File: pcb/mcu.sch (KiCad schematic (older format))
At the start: 33 parts, among them J4 SWD Programming Header, J5 Conn_01x16_Male, J6 Conn_01x16_Male, Q1 2N7002, Q2 2N7002, Q3 2N7002, Q4 2N7002, SW1 Rotary_Encoder_Switch, U2 LM1117-3.3, U3 ﻿STM32L010C6

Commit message: PCB updates
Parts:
- added R7, R9: 10k, Resistor_SMD:R_0603_1608Metric, symbol Device:R
- added TP1: TestPoint, TestPoint:TestPoint_Pad_2.0x2.0mm, symbol Connector:TestPoint
- C18, C20, C21: value C -> 10n
- J5, J6: footprint Connector_PinHeader_2.54mm:PinHeader_1x16_P2.54mm_Vertical -> Connector_PinHeader_2.54mm:PinHeader_2x08_P2.54mm_Vertical
- R2, R3, R4: value R -> 10k; footprint (none) -> Resistor_SMD:R_0603_1608Metric
- SW1: footprint (none) -> Rotary_Encoder:RotaryEncoder_Alps_EC11E-Switch_Vertical_H20mm_CircularMountingHoles
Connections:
- net +3V3: now also R7.2, R9.2; no longer C18.1
- net GND: now also C18.2
- net SW: now also C18.1; no longer C18.2
- net ~RST: now also TP1.1
- net at R4.2, SW1.A: now also R9.1
- net at R3.2, SW1.B: now also R7.1
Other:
- moved on the sheet: C18
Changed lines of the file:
@@
 $Descr A4 11693 8268
 encoding utf-8
-Sheet 3 3
+Sheet 3 4
 Title ""
 Date ""
@@
 F 0 "SW1" H 2250 5083 50  0000 C CNN
 F 1 "Rotary_Encoder_Switch" H 2250 5174 50  0000 C CNN
-F 2 "" H 2100 5610 50  0001 C CNN
+F 2 "Rotary_Encoder:RotaryEncoder_Alps_EC11E-Switch_Vertical_H20mm_CircularMountingHoles" H 2100 5610 50  0001 C CNN
 F 3 "~" H 2250 5710 50  0001 C CNN
 	1    2250 5450
@@
 P 2950 5350
 F 0 "R3" V 2743 5350 50  0000 C CNN
-F 1 "R" V 2834 5350 50  0000 C CNN
-F 2 "" V 2880 5350 50  0001 C CNN
+F 1 "10k" V 2834 5350 50  0000 C CNN
+F 2 "Resistor_SMD:R_0603_1608Metric" V 2880 5350 50  0001 C CNN
 F 3 "~" H 2950 5350 50  0001 C CNN
 	1    2950 5350
@@
 P 2950 5550
 F 0 "R4" V 2743 5550 50  0000 C CNN
-F 1 "R" V 2834 5550 50  0000 C CNN
-F 2 "" V 2880 5550 50  0001 C CNN
+F 1 "10k" V 2834 5550 50  0000 C CNN
+F 2 "Resistor_SMD:R_0603_1608Metric" V 2880 5550 50  0001 C CNN
 F 3 "~" H 2950 5550 50  0001 C CNN
 	1    2950 5550
@@
 $EndComp
 Wire Wire Line
-	2550 5350 2800 5350
-Wire Wire Line
-	2550 5550 2800 5550
+	2550 5350 2600 5350
+Wire Wire Line
+	2550 5550 2700 5550
 $Comp
 L Device:C C20
@@
 P 3200 5700
 F 0 "C20" H 3315 5746 50  0000 L CNN
-F 1 "C" H 3315 5655 50  0000 L CNN
+F 1 "10n" H 3315 5655 50  0000 L CNN
 F 2 "Capacitor_SMD:C_0603_1608Metric" H 3238 5550 50  0001 C CNN
 F 3 "~" H 3200 5700 50  0001 C CNN
@@
 P 3600 5700
 F 0 "C21" H 3715 5746 50  0000 L CNN
-F 1 "C" H 3715 5655 50  0000 L CNN
+F 1 "10n" H 3715 5655 50  0000 L CNN
 F 2 "Capacitor_SMD:C_0603_1608Metric" H 3638 5550 50  0001 C CNN
 F 3 "~" H 3600 5700 50  0001 C CNN
@@
 P 1800 5000
 F 0 "R2" H 1730 4954 50  0000 R CNN
-F 1 "R" H 1730 5045 50  0000 R CNN
-F 2 "" V 1730 5000 50  0001 C CNN
+F 1 "10k" H 1730 5045 50  0000 R CNN
+F 2 "Resistor_SMD:R_0603_1608Metric" V 1730 5000 50  0001 C CNN
 F 3 "~" H 1800 5000 50  0001 C CNN
 	1    1800 5000
@@
 L Device:C C18
 U 1 1 61337D20
-P 1500 5000
-F 0 "C18" H 1615 5046 50  0000 L CNN
-F 1 "C" H 1615 4955 50  0000 L CNN
-F 2 "Capacitor_SMD:C_0603_1608Metric" H 1538 4850 50  0001 C CNN
-F 3 "~" H 1500 5000 50  0001 C CNN
-	1    1500 5000
+P 1650 5500
+F 0 "C18" H 1765 5546 50  0000 L CNN
+F 1 "10n" H 1765 5455 50  0000 L CNN
+F 2 "Capacitor_SMD:C_0603_1608Metric" H 1688 5350 50  0001 C CNN
+F 3 "~" H 1650 5500 50  0001 C CNN
+	1    1650 5500
 	1    0    0    -1
 $EndComp
@@
 Wire Wire Line
 	1800 5350 1800 5150
-Wire Wire Line
-	1500 5150 1800 5150
-Wire Wire Line
-	1500 4850 1800 4850
 $Comp
 L power:+3.3V #PWR023
@@
 	1    0    0    -1
 $EndComp
-Connection ~ 1800 4850
 Text Label 1500 5350 0    50   ~ 0
 SW
 Wire Wire Line
-	1500 5350 1800 5350
+	1500 5350 1650 5350
 Connection ~ 1800 5350
 Text Label 3150 5550 0    50   ~ 0
@@
 F 0 "J6" H 7422 3724 50  0000 R CNN
 F 1 "Conn_01x16_Male" H 7422 3633 50  0000 R CNN
-F 2 "Connector_PinHeader_2.54mm:PinHeader_1x16_P2.54mm_Vertical" H 7450 3750 50  0001 C CNN
+F 2 "Connector_PinHeader_2.54mm:PinHeader_2x08_P2.54mm_Vertical" H 7450 3750 50  0001 C CNN
 F 3 "~" H 7450 3750 50  0001 C CNN
 	1    7450 3750
@@
 Wire Wire Line
 	7250 4550 6700 4550
-Connection ~ 1800 5150
 $Comp
 L Connector:Conn_01x16_Male J5
@@
 F 0 "J5" H 3608 4631 50  0000 C CNN
 F 1 "Conn_01x16_Male" H 3608 4540 50  0000 C CNN
-F 2 "Connector_PinHeader_2.54mm:PinHeader_1x16_P2.54mm_Vertical" H 3500 3750 50  0001 C CNN
+F 2 "Connector_PinHeader_2.54mm:PinHeader_2x08_P2.54mm_Vertical" H 3500 3750 50  0001 C CNN
 F 3 "~" H 3500 3750 50  0001 C CNN
 	1    3500 3750
@@
 Wire Wire Line
 	4200 1650 4450 1650
+$Comp
+L Connector:TestPoint TP1
+U 1 1 613DAC52
+P 5800 1350
+F 0 "TP1" H 5858 1468 50  0000 L CNN
+F 1 "TestPoint" H 5858 1377 50  0000 L CNN
+F 2 "TestPoint:TestPoint_Pad_2.0x2.0mm" H 6000 1350 50  0001 C CNN
+F 3 "~" H 6000 1350 50  0001 C CNN
+	1    5800 1350
+	1    0    0    -1
+$EndComp
+$Comp
+L Device:R R7
+U 1 1 613E9042
+P 2600 5200
+F 0 "R7" V 2393 5200 50  0000 C CNN
+F 1 "10k" V 2484 5200 50  0000 C CNN
+F 2 "Resistor_SMD:R_0603_1608Metric" V 2530 5200 50  0001 C CNN
+F 3 "~" H 2600 5200 50  0001 C CNN
+	1    2600 5200
+	-1   0    0    1
+$EndComp
+Connection ~ 2600 5350
+Wire Wire Line
+	2600 5350 2800 5350
+$Comp
+L Device:R R9
+U 1 1 613E96FC
+P 2700 5400
+F 0 "R9" V 2493 5400 50  0000 C CNN
+F 1 "10k" V 2584 5400 50  0000 C CNN
+F 2 "Resistor_SMD:R_0603_1608Metric" V 2630 5400 50  0001 C CNN
+F 3 "~" H 2700 5400 50  0001 C CNN
+	1    2700 5400
+	-1   0    0    1
+$EndComp
+Connection ~ 2700 5550
+Wire Wire Line
+	2700 5550 2800 5550
+$Comp
+L power:+3.3V #PWR0103
+U 1 1 613EA3BC
+P 2600 4900
+F 0 "#PWR0103" H 2600 4750 50  0001 C CNN
+F 1 "+3.3V" H 2615 5073 50  0000 C CNN
+F 2 "" H 2600 4900 50  0001 C CNN
+F 3 "" H 2600 4900 50  0001 C CNN
+	1    2600 4900
+	1    0    0    -1
+$EndComp
+Wire Wire Line
+	2600 5050 2600 4900
+Wire Wire Line
+	2700 5250 2700 4900
+Wire Wire Line
+	2700 4900 2600 4900
+Connection ~ 2600 4900
+Connection ~ 1650 5350
+Wire Wire Line
+	1650 5350 1800 5350
+Wire Wire Line
+	1650 5650 1750 5650
+Wire Wire Line
+	1750 5650 1750 5600
+Wire Wire Line
+	1750 5600 1800 5600
+Connection ~ 1800 5600
 $EndSCHEMATC

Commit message: layout check in
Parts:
- removed J5, J6: Conn_01x16_Male, Connector_PinHeader_2.54mm:PinHeader_2x08_P2.54mm_Vertical, symbol Connector:Conn_01x16_Male
- added J5: Conn_02x04_Odd_Even, Connector_PinHeader_2.54mm:PinHeader_2x04_P2.54mm_Vertical, symbol Connector_Generic:Conn_02x04_Odd_Even
- C17, C18, C19, C20, C21, C22, C23, C24, C25: footprint Capacitor_SMD:C_0603_1608Metric -> Capacitor_SMD:C_0402_1005Metric
- R10, R12, R14, R15, R16, R17, R18, R2, R3, R4, R5, R6, R7, R8, R9: footprint Resistor_SMD:R_0603_1608Metric -> Resistor_SMD:R_0402_1005Metric
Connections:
- wire segments 81 -> 103
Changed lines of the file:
@@
 F 0 "C19" H 2365 1246 50  0000 L CNN
 F 1 "1u" H 2365 1155 50  0000 L CNN
-F 2 "Capacitor_SMD:C_0603_1608Metric" H 2288 1050 50  0001 C CNN
+F 2 "Capacitor_SMD:C_0402_1005Metric" H 2288 1050 50  0001 C CNN
 F 3 "~" H 2250 1200 50  0001 C CNN
 	1    2250 1200
@@
 F 0 "C17" H 1365 1246 50  0000 L CNN
 F 1 "1u" H 1365 1155 50  0000 L CNN
-F 2 "Capacitor_SMD:C_0603_1608Metric" H 1288 1050 50  0001 C CNN
+F 2 "Capacitor_SMD:C_0402_1005Metric" H 1288 1050 50  0001 C CNN
 F 3 "~" H 1250 1200 50  0001 C CNN
 	1    1250 1200
@@
 F 0 "C23" H 4815 1546 50  0000 L CNN
 F 1 "100n" H 4815 1455 50  0000 L CNN
-F 2 "Capacitor_SMD:C_0603_1608Metric" H 4738 1350 50  0001 C CNN
+F 2 "Capacitor_SMD:C_0402_1005Metric" H 4738 1350 50  0001 C CNN
 F 3 "~" H 4700 1500 50  0001 C CNN
 	1    4700 1500
@@
 F 0 "C22" H 4565 1546 50  0000 L CNN
 F 1 "100n" H 4565 1455 50  0000 L CNN
-F 2 "Capacitor_SMD:C_0603_1608Metric" H 4488 1350 50  0001 C CNN
+F 2 "Capacitor_SMD:C_0402_1005Metric" H 4488 1350 50  0001 C CNN
 F 3 "~" H 4450 1500 50  0001 C CNN
 	1    4450 1500
@@
 F 0 "R3" V 2743 5350 50  0000 C CNN
 F 1 "10k" V 2834 5350 50  0000 C CNN
-F 2 "Resistor_SMD:R_0603_1608Metric" V 2880 5350 50  0001 C CNN
+F 2 "Resistor_SMD:R_0402_1005Metric" V 2880 5350 50  0001 C CNN
 F 3 "~" H 2950 5350 50  0001 C CNN
 	1    2950 5350
@@
 F 0 "R4" V 2743 5550 50  0000 C CNN
 F 1 "10k" V 2834 5550 50  0000 C CNN
-F 2 "Resistor_SMD:R_0603_1608Metric" V 2880 5550 50  0001 C CNN
+F 2 "Resistor_SMD:R_0402_1005Metric" V 2880 5550 50  0001 C CNN
 F 3 "~" H 2950 5550 50  0001 C CNN
 	1    2950 5550
@@
 F 0 "C20" H 3315 5746 50  0000 L CNN
 F 1 "10n" H 3315 5655 50  0000 L CNN
-F 2 "Capacitor_SMD:C_0603_1608Metric" H 3238 5550 50  0001 C CNN
+F 2 "Capacitor_SMD:C_0402_1005Metric" H 3238 5550 50  0001 C CNN
 F 3 "~" H 3200 5700 50  0001 C CNN
 	1    3200 5700
@@
 F 0 "C21" H 3715 5746 50  0000 L CNN
 F 1 "10n" H 3715 5655 50  0000 L CNN
-F 2 "Capacitor_SMD:C_0603_1608Metric" H 3638 5550 50  0001 C CNN
+F 2 "Capacitor_SMD:C_0402_1005Metric" H 3638 5550 50  0001 C CNN
 F 3 "~" H 3600 5700 50  0001 C CNN
 	1    3600 5700
@@
 F 0 "R2" H 1730 4954 50  0000 R CNN
 F 1 "10k" H 1730 5045 50  0000 R CNN
-F 2 "Resistor_SMD:R_0603_1608Metric" V 1730 5000 50  0001 C CNN
+F 2 "Resistor_SMD:R_0402_1005Metric" V 1730 5000 50  0001 C CNN
 F 3 "~" H 1800 5000 50  0001 C CNN
 	1    1800 5000
@@
 F 0 "C18" H 1765 5546 50  0000 L CNN
 F 1 "10n" H 1765 5455 50  0000 L CNN
-F 2 "Capacitor_SMD:C_0603_1608Metric" H 1688 5350 50  0001 C CNN
+F 2 "Capacitor_SMD:C_0402_1005Metric" H 1688 5350 50  0001 C CNN
 F 3 "~" H 1650 5500 50  0001 C CNN
 	1    1650 5500
@@
 F 0 "C24" H 5765 1546 50  0000 L CNN
 F 1 "0.1u" H 5765 1455 50  0000 L CNN
-F 2 "Capacitor_SMD:C_0603_1608Metric" H 5688 1350 50  0001 C CNN
+F 2 "Capacitor_SMD:C_0402_1005Metric" H 5688 1350 50  0001 C CNN
 F 3 "~" H 5650 1500 50  0001 C CNN
 	1    5650 1500
@@
 F 0 "R5" H 9320 1246 50  0000 L CNN
 F 1 "82" H 9320 1155 50  0000 L CNN
-F 2 "Resistor_SMD:R_0603_1608Metric" V 9180 1200 50  0001 C CNN
+F 2 "Resistor_SMD:R_0402_1005Metric" V 9180 1200 50  0001 C CNN
 F 3 "~" H 9250 1200 50  0001 C CNN
 	1    9250 1200
@@
 F 0 "R6" H 9420 1246 50  0000 L CNN
 F 1 "82" H 9420 1155 50  0000 L CNN
-F 2 "Resistor_SMD:R_0603_1608Metric" V 9280 1200 50  0001 C CNN
+F 2 "Resistor_SMD:R_0402_1005Metric" V 9280 1200 50  0001 C CNN
 F 3 "~" H 9350 1200 50  0001 C CNN
 	1    9350 1200
@@
 F 0 "R8" H 9520 1246 50  0000 L CNN
 F 1 "82" H 9520 1155 50  0000 L CNN
-F 2 "Resistor_SMD:R_0603_1608Metric" V 9380 1200 50  0001 C CNN
+F 2 "Resistor_SMD:R_0402_1005Metric" V 9380 1200 50  0001 C CNN
 F 3 "~" H 9450 1200 50  0001 C CNN
 	1    9450 1200
@@
 F 0 "R10" H 9620 1246 50  0000 L CNN
 F 1 "82" H 9620 1155 50  0000 L CNN
-F 2 "Resistor_SMD:R_0603_1608Metric" V 9480 1200 50  0001 C CNN
+F 2 "Resistor_SMD:R_0402_1005Metric" V 9480 1200 50  0001 C CNN
 F 3 "~" H 9550 1200 50  0001 C CNN
 	1    9550 1200
@@
 F 0 "R12" H 9720 1246 50  0000 L CNN
 F 1 "82" H 9720 1155 50  0000 L CNN
-F 2 "Resistor_SMD:R_0603_1608Metric" V 9580 1200 50  0001 C CNN
+F 2 "Resistor_SMD:R_0402_1005Metric" V 9580 1200 50  0001 C CNN
 F 3 "~" H 9650 1200 50  0001 C CNN
 	1    9650 1200
@@
 F 0 "R14" H 9820 1246 50  0000 L CNN
 F 1 "82" H 9820 1155 50  0000 L CNN
-F 2 "Resistor_SMD:R_0603_1608Metric" V 9680 1200 50  0001 C CNN
+F 2 "Resistor_SMD:R_0402_1005Metric" V 9680 1200 50  0001 C CNN
 F 3 "~" H 9750 1200 50  0001 C CNN
 	1    9750 1200
@@
 F 0 "R15" H 9920 1246 50  0000 L CNN
 F 1 "82" H 9920 1155 50  0000 L CNN
-F 2 "Resistor_SMD:R_0603_1608Metric" V 9780 1200 50  0001 C CNN
+F 2 "Resistor_SMD:R_0402_1005Metric" V 9780 1200 50  0001 C CNN
 F 3 "~" H 9850 1200 50  0001 C CNN
 	1    9850 1200
@@
 F 0 "R16" H 10020 1246 50  0000 L CNN
 F 1 "82" H 10020 1155 50  0000 L CNN
-F 2 "Resistor_SMD:R_0603_1608Metric" V 9880 1200 50  0001 C CNN
+F 2 "Resistor_SMD:R_0402_1005Metric" V 9880 1200 50  0001 C CNN
 F 3 "~" H 9950 1200 50  0001 C CNN
 	1    9950 1200
@@
 F 0 "R17" H 10120 1246 50  0000 L CNN
 F 1 "82" H 10120 1155 50  0000 L CNN
-F 2 "Resistor_SMD:R_0603_1608Metric" V 9980 1200 50  0001 C CNN
+F 2 "Resistor_SMD:R_0402_1005Metric" V 9980 1200 50  0001 C CNN
 F 3 "~" H 10050 1200 50  0001 C CNN
 	1    10050 1200
@@
 F 0 "R18" H 10220 1246 50  0000 L CNN
 F 1 "82" H 10220 1155 50  0000 L CNN
-F 2 "Resistor_SMD:R_0603_1608Metric" V 10080 1200 50  0001 C CNN
+F 2 "Resistor_SMD:R_0402_1005Metric" V 10080 1200 50  0001 C CNN
 F 3 "~" H 10150 1200 50  0001 C CNN
 	1    10150 1200
@@
 Text Label 6700 4350 0    50   ~ 0
 DIG4
-$Comp
-L Connector:Conn_01x16_Male J6
-U 1 1 613A74A3
-P 7450 3750
-F 0 "J6" H 7422 3724 50  0000 R CNN
-F 1 "Conn_01x16_Male" H 7422 3633 50  0000 R CNN
-F 2 "Connector_PinHeader_2.54mm:PinHeader_2x08_P2.54mm_Vertical" H 7450 3750 50  0001 C CNN
-F 3 "~" H 7450 3750 50  0001 C CNN
-	1    7450 3750
-	-1   0    0    -1
-$EndComp
 Wire Wire Line
 	7250 3050 6700 3050
@@
 Wire Wire Line
 	7250 4550 6700 4550
-$Comp
-L Connector:Conn_01x16_Male J5
-U 1 1 613C1375
-P 3500 3750
-F 0 "J5" H 3608 4631 50  0000 C CNN
-F 1 "Conn_01x16_Male" H 3608 4540 50  0000 C CNN
-F 2 "Connector_PinHeader_2.54mm:PinHeader_2x08_P2.54mm_Vertical" H 3500 3750 50  0001 C CNN
-F 3 "~" H 3500 3750 50  0001 C CNN
-	1    3500 3750
-	1    0    0    -1
-$EndComp
-Wire Wire Line
-	3700 3050 4600 3050
-Wire Wire Line
-	3700 3150 4600 3150
-Wire Wire Line
-	4600 3250 3700 3250
-Wire Wire Line
-	3700 3350 4600 3350
-Wire Wire Line
-	4600 3450 3700 3450
-Wire Wire Line
-	3700 3550 4600 3550
-Wire Wire Line
-	3700 3650 4600 3650
-Wire Wire Line
-	4600 3750 3700 3750
 Wire Wire Line
 	3700 3850 4600 3850
 Wire Wire Line
 	4600 3950 3700 3950
-Wire Wire Line
-	3700 4050 4600 4050
-Wire Wire Line
-	4600 4150 3700 4150
-Wire Wire Line
-	3700 4250 4600 4250
-Wire Wire Line
-	3700 4350 4600 4350
-Wire Wire Line
-	3700 4450 4600 4450
-Wire Wire Line
-	3750 4550 4600 4550
 $Comp
 L Device:C C25
@@
 F 0 "C25" H 4315 1546 50  0000 L CNN
 F 1 "100n" H 4315 1455 50  0000 L CNN
-F 2 "Capacitor_SMD:C_0603_1608Metric" H 4238 1350 50  0001 C CNN
+F 2 "Capacitor_SMD:C_0402_1005Metric" H 4238 1350 50  0001 C CNN
 F 3 "~" H 4200 1500 50  0001 C CNN
 	1    4200 1500
@@
 F 0 "R7" V 2393 5200 50  0000 C CNN
 F 1 "10k" V 2484 5200 50  0000 C CNN
-F 2 "Resistor_SMD:R_0603_1608Metric" V 2530 5200 50  0001 C CNN
+F 2 "Resistor_SMD:R_0402_1005Metric" V 2530 5200 50  0001 C CNN
 F 3 "~" H 2600 5200 50  0001 C CNN
 	1    2600 5200
@@
 F 0 "R9" V 2493 5400 50  0000 C CNN
 F 1 "10k" V 2584 5400 50  0000 C CNN
-F 2 "Resistor_SMD:R_0603_1608Metric" V 2630 5400 50  0001 C CNN
+F 2 "Resistor_SMD:R_0402_1005Metric" V 2630 5400 50  0001 C CNN
 F 3 "~" H 2700 5400 50  0001 C CNN
 	1    2700 5400
@@
 	1750 5600 1800 5600
 Connection ~ 1800 5600
+Wire Wire Line
+	2600 3550 4600 3550
+Wire Wire Line
+	2700 3650 4600 3650
+Wire Wire Line
+	2800 3750 2800 3850
+Wire Wire Line
+	2800 3750 4600 3750
+Wire Wire Line
+	2700 3650 2700 3850
+Wire Wire Line
+	2600 3550 2600 3850
+Wire Wire Line
+	2600 4350 2600 4600
+Wire Wire Line
+	2600 4600 3700 4600
+Wire Wire Line
+	3700 4600 3700 4550
+Wire Wire Line
+	2700 4550 2700 4350
+Wire Wire Line
+	2800 4350 2800 4500
+Wire Wire Line
+	3700 3850 3700 3800
+Wire Wire Line
+	3700 3800 2900 3800
+Wire Wire Line
+	2900 3800 2900 3850
+Wire Wire Line
+	4300 4350 4600 4350
+Wire Wire Line
+	4600 4450 4300 4450
+Wire Wire Line
+	4600 3050 4350 3050
+Wire Wire Line
+	4600 3150 4350 3150
+Wire Wire Line
+	3650 4250 3650 4550
+Wire Wire Line
+	3650 4550 2700 4550
+Wire Wire Line
+	3650 4250 3800 4250
+Wire Wire Line
+	2800 4500 3600 4500
+Wire Wire Line
+	3600 4500 3600 4150
+Wire Wire Line
+	3400 4050 3400 4450
+Wire Wire Line
+	3400 4450 2900 4450
+Wire Wire Line
+	2900 4450 2900 4350
+$Comp
+L Connector_Generic:Conn_02x04_Odd_Even J5
+U 1 1 6155CAFE
+P 2700 4150
+F 0 "J5" V 2796 3862 50  0000 R CNN
+F 1 "Conn_02x04_Odd_Even" V 2705 3862 50  0000 R CNN
+F 2 "Connector_PinHeader_2.54mm:PinHeader_2x04_P2.54mm_Vertical" H 2700 4150 50  0001 C CNN
+F 3 "~" H 2700 4150 50  0001 C CNN
+	1    2700 4150
+	0    -1   -1   0
+$EndComp
+Wire Wire Line
+	3700 4050 3700 3950
+Wire Wire Line
+	3400 4050 3700 4050
+Wire Wire Line
+	4600 4050 3750 4050
+Wire Wire Line
+	3750 4050 3750 4150
+Wire Wire Line
+	3750 4150 3600 4150
+Wire Wire Line
+	4600 4150 3800 4150
+Wire Wire Line
+	3800 4150 3800 4250
+Wire Wire Line
+	3700 4550 3850 4550
+Wire Wire Line
+	4600 4250 3850 4250
+Wire Wire Line
+	3850 4250 3850 4550
 $EndSCHEMATC

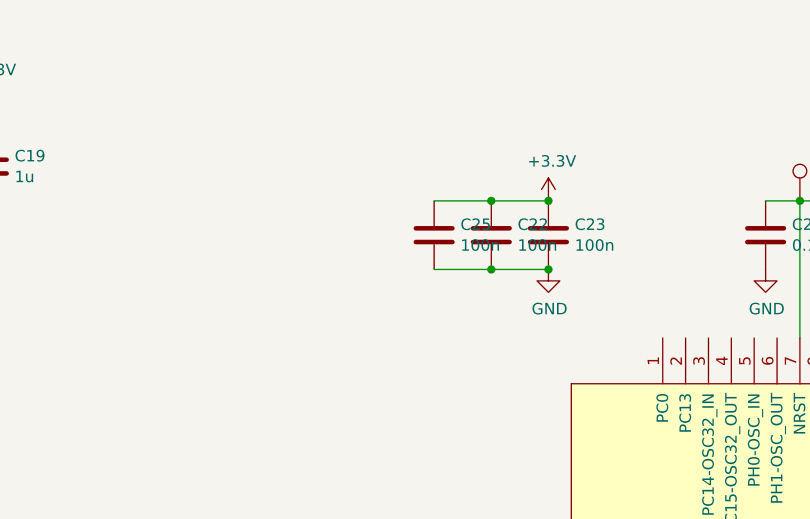
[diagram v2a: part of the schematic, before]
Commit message: Completed PCB layout
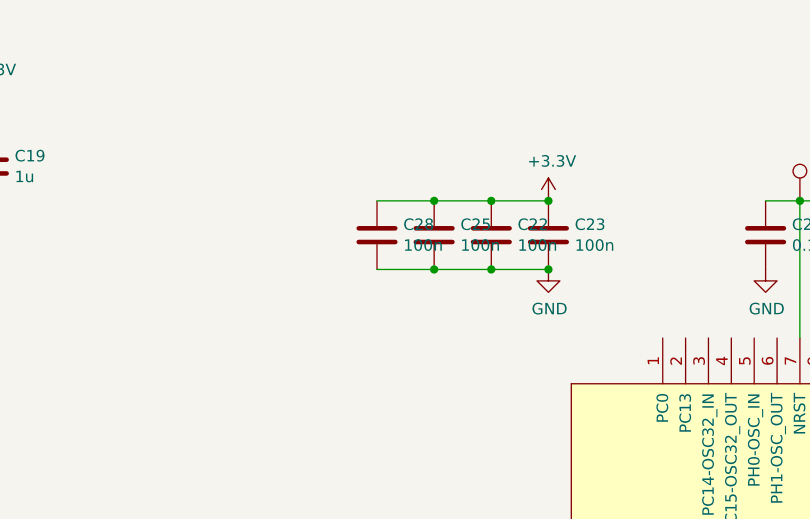
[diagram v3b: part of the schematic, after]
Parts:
- added C28: 100n, Capacitor_SMD:C_0402_1005Metric, symbol Device:C
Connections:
- wire segments 103 -> 105
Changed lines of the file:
@@
 Wire Wire Line
 	3850 4250 3850 4550
+$Comp
+L Device:C C28
+U 1 1 61460616
+P 3950 1500
+F 0 "C28" H 4065 1546 50  0000 L CNN
+F 1 "100n" H 4065 1455 50  0000 L CNN
+F 2 "Capacitor_SMD:C_0402_1005Metric" H 3988 1350 50  0001 C CNN
+F 3 "~" H 3950 1500 50  0001 C CNN
+	1    3950 1500
+	1    0    0    -1
+$EndComp
+Wire Wire Line
+	3950 1350 4200 1350
+Connection ~ 4200 1350
+Wire Wire Line
+	3950 1650 4200 1650
+Connection ~ 4200 1650
 $EndSCHEMATC

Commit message: final tweaks and produce outputs for jlcpcb fabrication
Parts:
- C22, C23, C25, C28: value 100n -> 0.1u
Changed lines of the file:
@@
 P 4700 1500
 F 0 "C23" H 4815 1546 50  0000 L CNN
-F 1 "100n" H 4815 1455 50  0000 L CNN
+F 1 "0.1u" H 4815 1455 50  0000 L CNN
 F 2 "Capacitor_SMD:C_0402_1005Metric" H 4738 1350 50  0001 C CNN
 F 3 "~" H 4700 1500 50  0001 C CNN
@@
 P 4450 1500
 F 0 "C22" H 4565 1546 50  0000 L CNN
-F 1 "100n" H 4565 1455 50  0000 L CNN
+F 1 "0.1u" H 4565 1455 50  0000 L CNN
 F 2 "Capacitor_SMD:C_0402_1005Metric" H 4488 1350 50  0001 C CNN
 F 3 "~" H 4450 1500 50  0001 C CNN
@@
 P 4200 1500
 F 0 "C25" H 4315 1546 50  0000 L CNN
-F 1 "100n" H 4315 1455 50  0000 L CNN
+F 1 "0.1u" H 4315 1455 50  0000 L CNN
 F 2 "Capacitor_SMD:C_0402_1005Metric" H 4238 1350 50  0001 C CNN
 F 3 "~" H 4200 1500 50  0001 C CNN
@@
 P 3950 1500
 F 0 "C28" H 4065 1546 50  0000 L CNN
-F 1 "100n" H 4065 1455 50  0000 L CNN
+F 1 "0.1u" H 4065 1455 50  0000 L CNN
 F 2 "Capacitor_SMD:C_0402_1005Metric" H 3988 1350 50  0001 C CNN
 F 3 "~" H 3950 1500 50  0001 C CNN
@@
 	3950 1650 4200 1650
 Connection ~ 4200 1650
+$Comp
+L power:+3.3V #PWR?
+U 1 1 614E75B2
+P 5200 1950
+F 0 "#PWR?" H 5200 1800 50  0001 C CNN
+F 1 "+3.3V" H 5215 2123 50  0000 C CNN
+F 2 "" H 5200 1950 50  0001 C CNN
+F 3 "" H 5200 1950 50  0001 C CNN
+	1    5200 1950
+	1    0    0    -1
+$EndComp
 $EndSCHEMATC

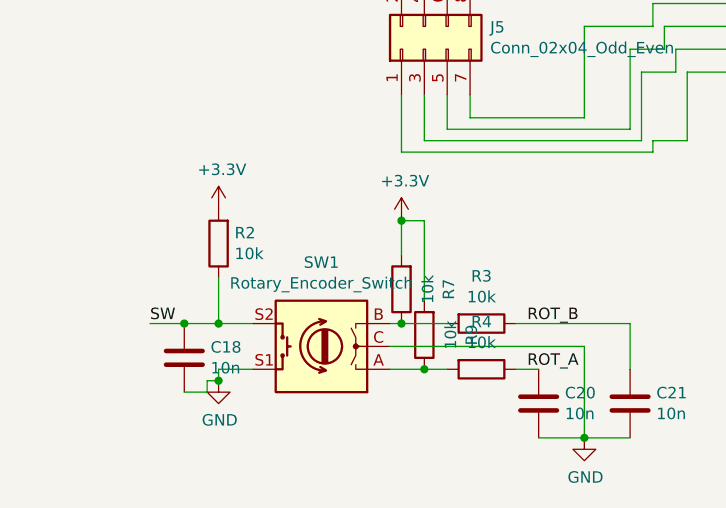
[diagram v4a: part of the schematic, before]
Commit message: Made a 3d printed case
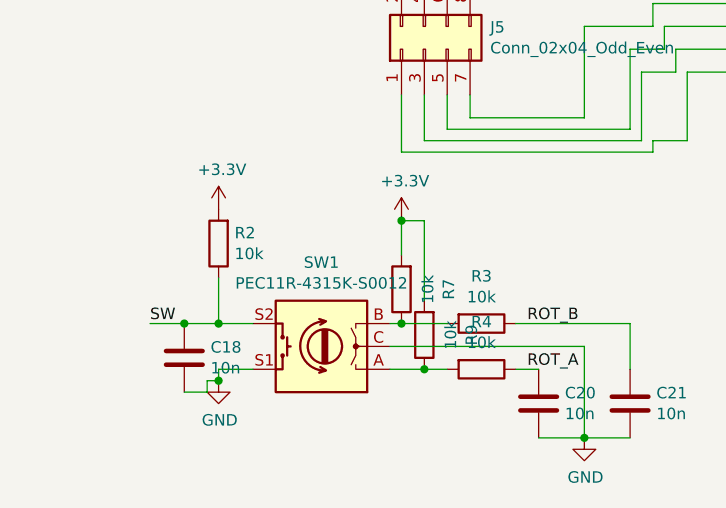
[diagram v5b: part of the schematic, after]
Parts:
- SW1: value Rotary_Encoder_Switch -> PEC11R-4315K-S0012
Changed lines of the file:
@@
 P 2250 5450
 F 0 "SW1" H 2250 5083 50  0000 C CNN
-F 1 "Rotary_Encoder_Switch" H 2250 5174 50  0000 C CNN
+F 1 "PEC11R-4315K-S0012" H 2250 5174 50  0000 C CNN
 F 2 "Rotary_Encoder:RotaryEncoder_Alps_EC11E-Switch_Vertical_H20mm_CircularMountingHoles" H 2100 5610 50  0001 C CNN
 F 3 "~" H 2250 5710 50  0001 C CNN
